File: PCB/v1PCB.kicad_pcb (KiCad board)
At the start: 2 copper layers, 369.9 x 122.3 mm, 218 parts, among them SW1 SW_PUSH, SW2 SW_PUSH, U1 STM32F072CBUx, U2 MCP1700-3302E_SOT23

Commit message: Removed ratsnest, need to fix all runs to vddio, need USB
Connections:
- C1 pad 2: +5V -> GND
- C10 pad 2: +5V -> GND
- C2 pad 2: +5V -> GND
- C3 pad 2: +5V -> GND
- C4 pad 2: +5V -> GND
- C5 pad 2: +5V -> GND
- C6 pad 2: +5V -> GND
- C7 pad 2: +5V -> GND
- C8 pad 2: +5V -> GND
- C9 pad 2: +5V -> GND
- R2 pad 2: +5V -> GND
- SW1 pad 2: +5V -> GND
- U1 pad 23: +5V -> GND
- U1 pad 35: +5V -> GND
- U1 pad 47: +5V -> GND
- U1 pad 49: +5V -> GND
- U1 pad 8: +5V -> GND
- U2 pad 1: +5V -> GND

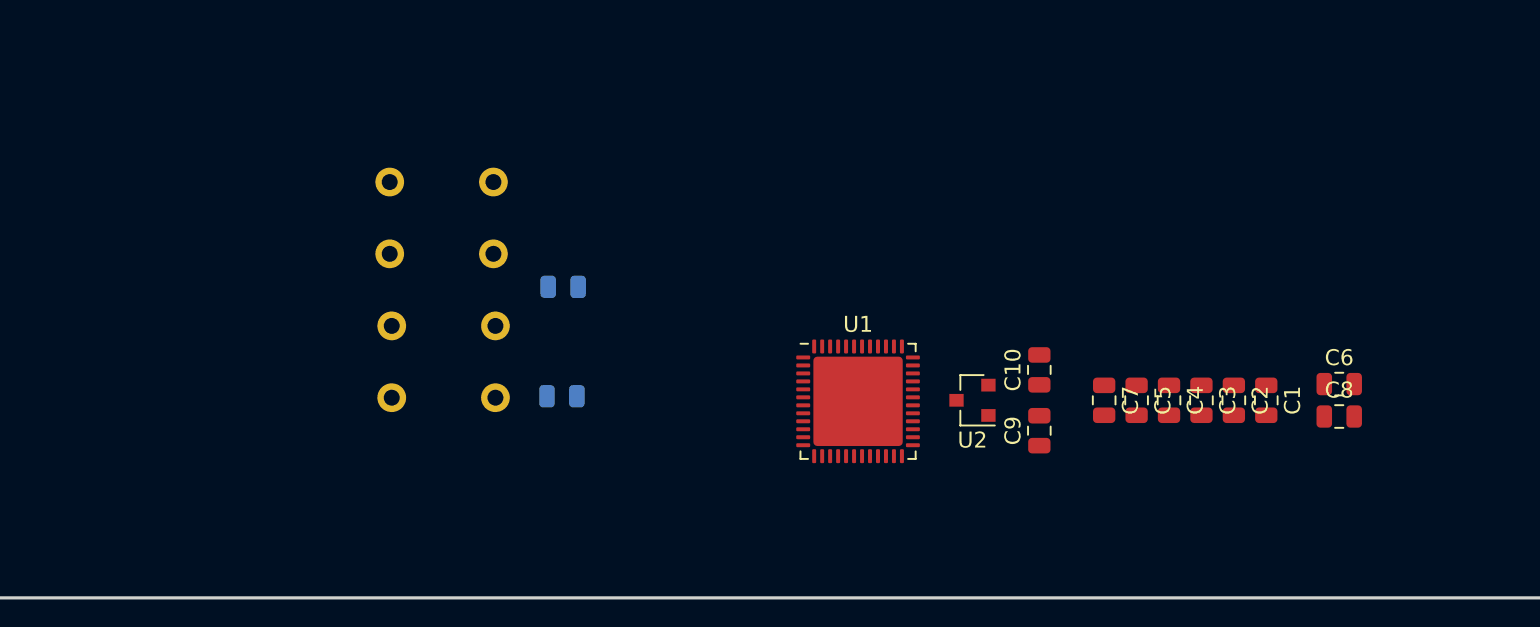
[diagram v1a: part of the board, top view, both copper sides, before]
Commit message: Fixed a few runs, still need to add USB and redo VDDIO decoupling capacitors
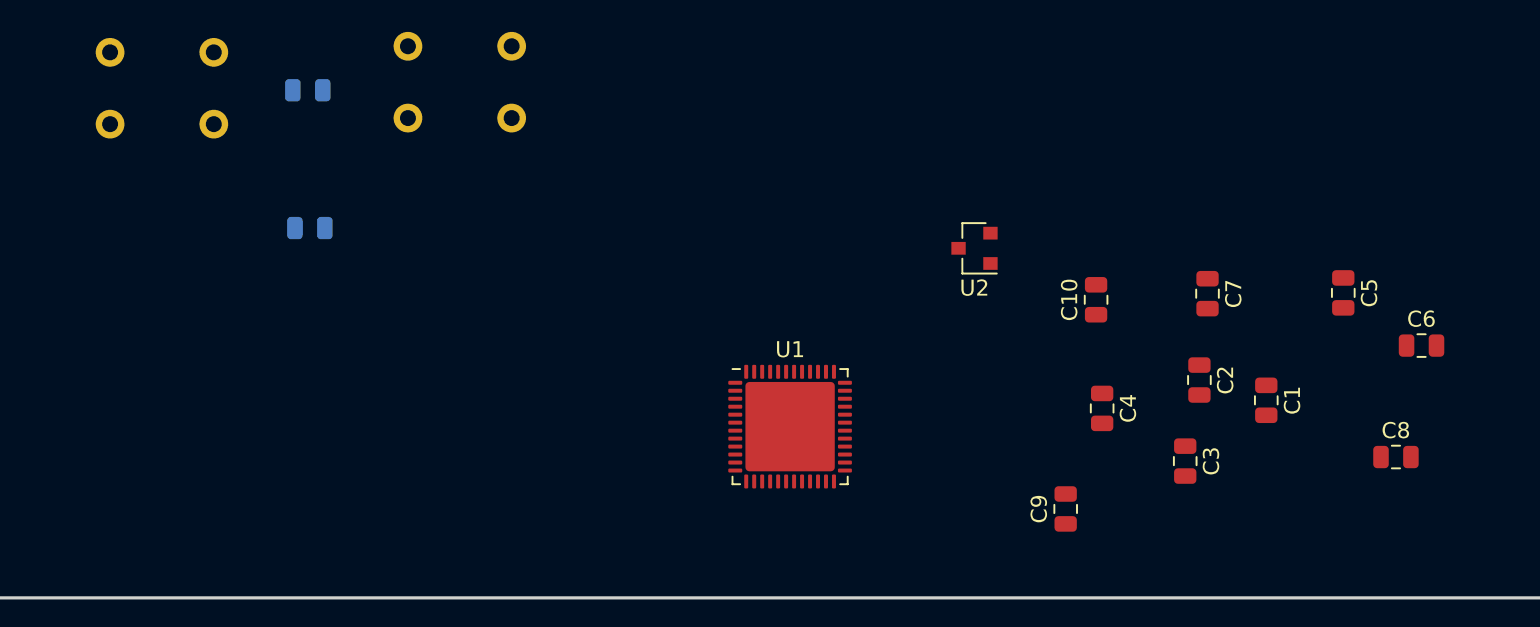
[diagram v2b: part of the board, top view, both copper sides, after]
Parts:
- moved R2 24.9 mm to (222.6, 71.0)
- moved SW2 24.6 mm to (213.5, 70.9)
- moved R1 16.3 mm to (222.8, 79.6)
- moved C5 14.6 mm to (287.5, 83.7)
- moved U2 9.53 mm to (264.4, 80.9)
- moved C7 9.31 mm to (279.0, 83.7)
- moved SW1 8.59 mm to (232.2, 70.5)
- moved C6 5.69 mm to (292.4, 87.0)
- moved C10 5.65 mm to (272.0, 84.1)
- moved C9 5.17 mm to (270.1, 97.2)
- moved U1 4.54 mm to (252.9, 92.1)
- moved C8 4.37 mm to (290.8, 94.0)
- moved C4 4.22 mm to (272.4, 90.9)
- moved C3 3.94 mm to (277.6, 94.2)
- moved C2 2.50 mm to (278.5, 89.2)
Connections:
- U1 pad 10: col16 -> row0
- U1 pad 11: col17 -> row1
- U1 pad 12: col18 -> row2
- U1 pad 13: row0 -> row3
- U1 pad 14: row1 -> row4
- U1 pad 15: row2 -> col8
- U1 pad 16: row3 -> col9
- U1 pad 17: row4 -> col10
- U1 pad 18: col0 -> row5
- U1 pad 19: col1 -> col0
- U1 pad 20: col2 -> col1
- U1 pad 21: col10 -> col2
- U1 pad 22: col11 -> col3
- U1 pad 25: col12 -> col4
- U1 pad 26: col13 -> col5
- U1 pad 27: col14 -> col6
- U1 pad 28: col15 -> col7
- U1 pad 29: row5 -> col11
- U1 pad 30: Net-(U1-Pad30) -> col12
- U1 pad 31: Net-(U1-Pad31) -> col16
- U1 pad 34: Net-(U1-Pad34) -> col17
- U1 pad 37: Net-(U1-Pad37) -> col18
- U1 pad 39: col3 -> Net-(U1-Pad39)
- U1 pad 40: col4 -> Net-(U1-Pad40)
- U1 pad 41: col5 -> Net-(U1-Pad41)
- U1 pad 42: col6 -> Net-(U1-Pad42)
- U1 pad 43: col7 -> Net-(U1-Pad43)
- U1 pad 45: col8 -> Net-(U1-Pad45)
- U1 pad 46: col9 -> Net-(U1-Pad46)

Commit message: Almost done with cap placement, still neeed to add USBC
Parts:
- removed C5: 100uF, Capacitor_SMD:C_0805_2012Metric
- moved R1 99.4 mm to (125.3, 99.4)
- moved R2 99.4 mm to (125.2, 90.8)
- moved SW1 99.4 mm to (134.7, 90.3)
- moved SW2 99.4 mm to (116.1, 90.7)
- moved C6 52.3 mm to (240.5, 93.2), turned to 90 degrees
- moved C8 45.9 mm to (245.0, 93.2), turned to 90 degrees
- moved C9 36.1 mm to (255.5, 64.3), turned to 180 degrees
- moved C1 28.6 mm to (255.4, 98.9), turned to 180 degrees
- moved C4 22.9 mm to (250.2, 85.5), turned to 0 degrees
- moved C7 19.6 mm to (262.8, 94.6)
- moved C3 17.9 mm to (260.4, 89.7)
- moved C10 16.1 mm to (256.9, 78.6), turned to 180 degrees
- moved U2 14.2 mm to (257.0, 68.7), turned to 90 degrees
- moved C2 13.4 mm to (265.1, 89.7)

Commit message: Finished schematic, begin drawing traces
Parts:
- added C5: 4.7nF, Capacitor_SMD:C_0603_1608Metric, F.Cu at (140.5, 108.0)
- added F1: Polyfuse, Fuse:Fuse_1206_3216Metric, B.Cu at (123.0, 106.4)
- added R3: 1M, Resistor_SMD:R_0805_2012Metric, F.Cu at (140.5, 105.6)
- added R4: 5.1k, Resistor_SMD:R_0805_2012Metric, F.Cu at (134.9, 112.7)
- added R5: 5.1k, Resistor_SMD:R_0805_2012Metric, F.Cu at (132.6, 112.7)
- added USB1: HRO-TYPE-C-31-M-12, Type-C:HRO-TYPE-C-31-M-12-Assembly, F.Cu at (133.3, 101.6)
- C1, C3, C4: value 100uF -> 100nF; footprint Capacitor_SMD:C_0805_2012Metric -> Capacitor_SMD:C_0402_1005Metric
- C10: footprint Capacitor_SMD:C_0805_2012Metric -> Capacitor_SMD:C_0402_1005Metric
- C2, C6, C7: footprint Capacitor_SMD:C_0805_2012Metric -> Capacitor_SMD:C_0603_1608Metric
- C8: value 10uF -> 10nF; footprint Capacitor_SMD:C_0805_2012Metric -> Capacitor_SMD:C_0402_1005Metric
- C9: footprint Capacitor_SMD:C_0805_2012Metric -> Capacitor_SMD:C_0402_1005Metric; moved to B.Cu
- K_0, K_1, K_10, K_100, K_11, K_12, K_13, K_14, K_15, K_16, K_17, K_18, K_19, K_2, K_20, K_21, K_22, K_23, K_24, K_25, K_26, K_27, K_28, K_29, K_3, K_30, K_31, K_33, K_34, K_35, K_36, K_38, K_39, K_4, K_40, K_41, K_42, K_43, K_44, K_45, K_46, K_47, K_48, K_49, K_5, K_51, K_52, K_53, K_54, K_56, K_57, K_58, K_59, K_6, K_60, K_61, K_62, K_63, K_64, K_65, K_66, K_68, K_69, K_7, K_70, K_72, K_73, K_74, K_75, K_76, K_77, K_78, K_79, K_8, K_80, K_81, K_83, K_84, K_85, K_86, K_87, K_9, K_96, K_97, K_98, K_99: footprint MX_Alps_Hybrid:MX-1U-NoLED -> MX_Only:MXOnly-1U-NoLED
- K_32: footprint MX_Alps_Hybrid:MX-2U-NoLED -> MX_Only:MXOnly-1U-NoLED
- K_37, K_50: footprint MX_Alps_Hybrid:MX-1.5U-NoLED -> MX_Only:MXOnly-1U-NoLED
- K_55, K_82: footprint MX_Alps_Hybrid:MX-1.75U-NoLED -> MX_Only:MXOnly-1U-NoLED
- K_67, K_71, K_91: footprint MX_Alps_Hybrid:MX-2.25U-NoLED -> MX_Only:MXOnly-1U-NoLED
- K_88, K_89, K_90, K_92, K_94, K_95: footprint MX_Alps_Hybrid:MX-1.25U-NoLED -> MX_Only:MXOnly-1U-NoLED
- K_93: footprint MX_Alps_Hybrid:MX-2.75U-NoLED -> MX_Only:MXOnly-1U-NoLED
- moved C9 156.4 mm to (282.6, 218.3), turned to 90 degrees
- moved U2 152.3 mm to (285.8, 218.3), turned to 0 degrees
- moved C10 143.5 mm to (289.7, 218.3), turned to 90 degrees
- moved C6 141.8 mm to (297.7, 223.0), turned to 180 degrees
- moved C4 139.0 mm to (291.3, 218.3), turned to 90 degrees
- moved C8 138.6 mm to (297.7, 221.5), turned to 180 degrees
- moved U1 131.4 mm to (296.9, 215.9), turned to 90 degrees
- moved C2 129.8 mm to (304.0, 213.5)
- moved C3 125.4 mm to (294.5, 210.3), turned to 0 degrees
- moved C1 123.9 mm to (302.4, 213.5), turned to 270 degrees
- moved C7 118.5 mm to (294.5, 208.8), turned to 0 degrees
- moved SW1 85.9 mm to (218.1, 69.7)
- moved SW2 85.9 mm to (199.4, 70.0)
- moved R1 85.9 mm to (208.7, 78.8)
- moved R2 85.9 mm to (208.6, 70.2)
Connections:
- U1 pad 10: row0 -> Net-(U1-Pad10)
- U1 pad 11: row1 -> Net-(U1-Pad11)
- U1 pad 12: row2 -> Net-(U1-Pad12)
- U1 pad 13: row3 -> Net-(U1-Pad13)
- U1 pad 14: row4 -> Net-(U1-Pad14)
- U1 pad 15: col8 -> Net-(U1-Pad15)
- U1 pad 16: col9 -> Net-(U1-Pad16)
- U1 pad 17: col10 -> Net-(U1-Pad17)
- U1 pad 18: row5 -> Net-(U1-Pad18)
- U1 pad 19: col0 -> Net-(U1-Pad19)
- U1 pad 20: col1 -> Net-(U1-Pad20)
- U1 pad 21: col2 -> Net-(U1-Pad21)
- U1 pad 22: col3 -> Net-(U1-Pad22)
- U1 pad 25: col4 -> Net-(U1-Pad25)
- U1 pad 26: col5 -> Net-(U1-Pad26)
- U1 pad 27: col6 -> Net-(U1-Pad27)
- U1 pad 28: col7 -> Net-(U1-Pad28)
- U1 pad 29: col11 -> Net-(U1-Pad29)
- U1 pad 30: col12 -> Net-(U1-Pad30)
- U1 pad 31: col16 -> Net-(U1-Pad31)
- U1 pad 34: col17 -> Net-(U1-Pad34)
- U1 pad 37: col18 -> Net-(U1-Pad37)
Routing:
- net GND: track 0.00 -> 651.9 mm, vias 0 -> 1
- net +5V: track 0.00 -> 295.6 mm
- net Net-(F1-Pad1): track 0.00 -> 11.4 mm, vias 0 -> 1
- net Net-(C5-Pad2): track 0.00 -> 4.66 mm
- net Net-(R5-Pad2): track 0.00 -> 2.88 mm
- net Net-(R4-Pad2): track 0.00 -> 2.62 mm

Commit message: Need to finish reset buttons, confirm routing of 3V3 and GND, review overall package
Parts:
- F1: value Polyfuse -> Polyfuse (1A)
- R4, R5, USB1: moved to B.Cu
- moved R1 169.4 mm to (300.0, 221.5), turned to 180 degrees
- moved R2 165.3 mm to (288.1, 215.1), turned to 90 degrees
- moved SW1 142.6 mm to (119.1, 172.2)
- moved SW2 122.7 mm to (119.3, 162.9), turned to 180 degrees
- moved D_93 19.4 mm to (269.1, 204.8), turned to 270 degrees
- moved C5 15.0 mm to (126.7, 101.9), turned to 0 degrees
- moved R3 13.8 mm to (126.7, 104.3), turned to 0 degrees
- moved D_67 11.7 mm to (387.4, 173.8)
- moved D_71 11.7 mm to (144.5, 193.0)
- moved D_32 9.32 mm to (389.7, 135.9)
- moved C3 6.95 mm to (294.5, 203.4)
- moved C7 6.95 mm to (294.5, 201.8)
- moved D_55 6.94 mm to (139.7, 173.8)
- moved D_82 6.94 mm to (373.1, 193.0)
- moved C9 6.05 mm to (277.0, 220.7)
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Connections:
- D_54 pad 1: row3 -> row2
- D_87 pad 1: row5 -> row4
- K_32 pad 1: col14 -> col13
- K_38 pad 1: col2 -> col1
- K_39 pad 1: col3 -> col2
- K_40 pad 1: col4 -> col3
- K_41 pad 1: col5 -> col4
- K_42 pad 1: col6 -> col5
- K_43 pad 1: col7 -> col6
- K_44 pad 1: col8 -> col7
- K_45 pad 1: col9 -> col8
- K_46 pad 1: col10 -> col9
- K_47 pad 1: col11 -> col10
- K_48 pad 1: col12 -> col11
- K_49 pad 1: col13 -> col12
- K_56 pad 1: col2 -> col1
- K_57 pad 1: col3 -> col2
- K_58 pad 1: col4 -> col3
- K_59 pad 1: col5 -> col4
- K_60 pad 1: col6 -> col5
- K_61 pad 1: col7 -> col6
- K_62 pad 1: col8 -> col7
- K_63 pad 1: col9 -> col8
- K_64 pad 1: col10 -> col9
- K_65 pad 1: col11 -> col10
- K_66 pad 1: col12 -> col11
- K_71 pad 1: col1 -> col0
- K_72 pad 1: col2 -> col1
- K_73 pad 1: col3 -> col2
- K_74 pad 1: col4 -> col3
- K_75 pad 1: col5 -> col4
- K_76 pad 1: col6 -> col5
- K_77 pad 1: col7 -> col6
- K_78 pad 1: col8 -> col7
- K_79 pad 1: col9 -> col8
- K_80 pad 1: col10 -> col9
- K_81 pad 1: col11 -> col10
- K_82 pad 1: col13 -> col12
- U1 pad 10: Net-(U1-Pad10) -> row0
- U1 pad 11: Net-(U1-Pad11) -> row1
- U1 pad 12: Net-(U1-Pad12) -> row2
- U1 pad 13: Net-(U1-Pad13) -> row3
- U1 pad 14: Net-(U1-Pad14) -> row4
- U1 pad 15: Net-(U1-Pad15) -> row5
- U1 pad 16: Net-(U1-Pad16) -> col18
- U1 pad 17: Net-(U1-Pad17) -> col17
- U1 pad 18: Net-(U1-Pad18) -> col16
- U1 pad 19: Net-(U1-Pad19) -> col15
- U1 pad 20: Net-(U1-Pad20) -> col14
- U1 pad 21: Net-(U1-Pad21) -> col13
- U1 pad 22: Net-(U1-Pad22) -> col12
- U1 pad 25: Net-(U1-Pad25) -> col11
- U1 pad 26: Net-(U1-Pad26) -> col10
- U1 pad 27: Net-(U1-Pad27) -> col9
- U1 pad 28: Net-(U1-Pad28) -> col8
- U1 pad 29: Net-(U1-Pad29) -> col7
- U1 pad 30: Net-(U1-Pad30) -> col6
- U1 pad 37: Net-(U1-Pad37) -> col5
- U1 pad 38: Net-(U1-Pad38) -> col4
- U1 pad 39: Net-(U1-Pad39) -> col3
- U1 pad 40: Net-(U1-Pad40) -> col2
- U1 pad 41: Net-(U1-Pad41) -> col1
- U1 pad 42: Net-(U1-Pad42) -> col0
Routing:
- net row0: track 0.00 -> 624.0 mm, vias 0 -> 1
- net row1: track 0.00 -> 601.9 mm, vias 0 -> 1
- net row2: track 0.00 -> 571.1 mm, vias 0 -> 1
- net row3: track 0.00 -> 551.5 mm, vias 0 -> 1
- net row4: track 0.00 -> 526.5 mm, vias 0 -> 1
- net row5: track 0.00 -> 494.7 mm, vias 0 -> 1
- net GND: track 651.9 -> 348.1 mm, vias 1 -> 4
- net D-: track 0.00 -> 290.3 mm, vias 0 -> 2
- net D+: track 0.00 -> 290.2 mm, vias 0 -> 1
- net col0: track 0.00 -> 280.7 mm
- net col1: track 0.00 -> 265.6 mm
- net col3: track 0.00 -> 260.1 mm
- net col18: track 0.00 -> 257.8 mm
- net col17: track 0.00 -> 243.8 mm
- net col2: track 0.00 -> 243.5 mm
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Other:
- board size 369.9 x 122.3 mm -> 370 x 125.1 mm
- net class Power: trace_width 0.381 -> 0.254

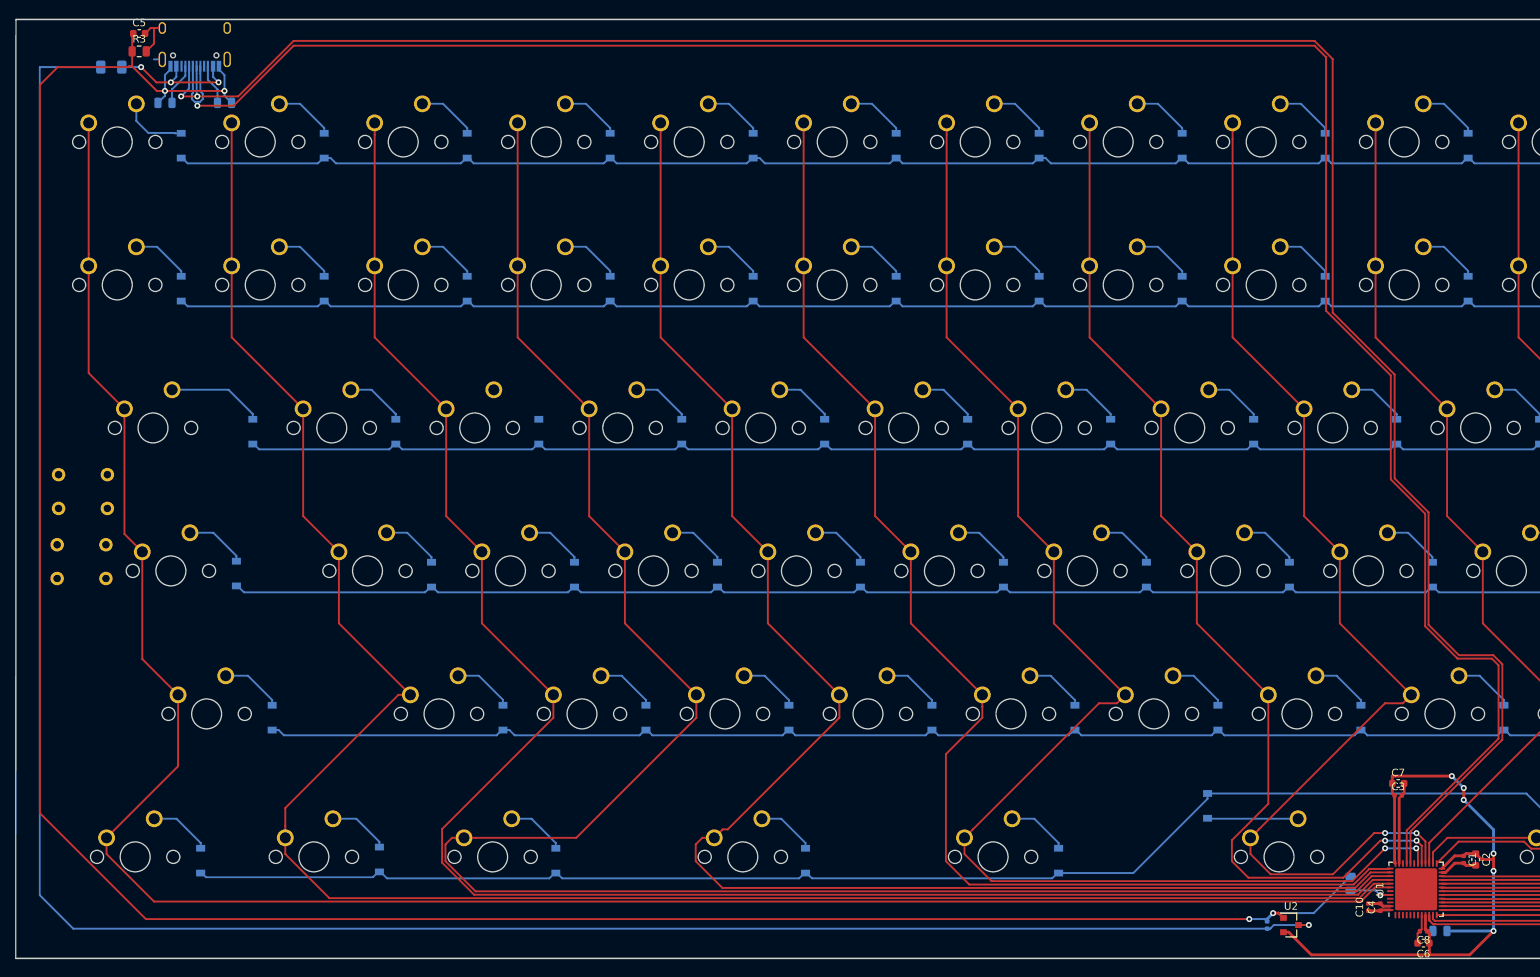
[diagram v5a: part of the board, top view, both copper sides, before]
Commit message: Added switches, fixed most DRC issues. Only questions about GNDleft
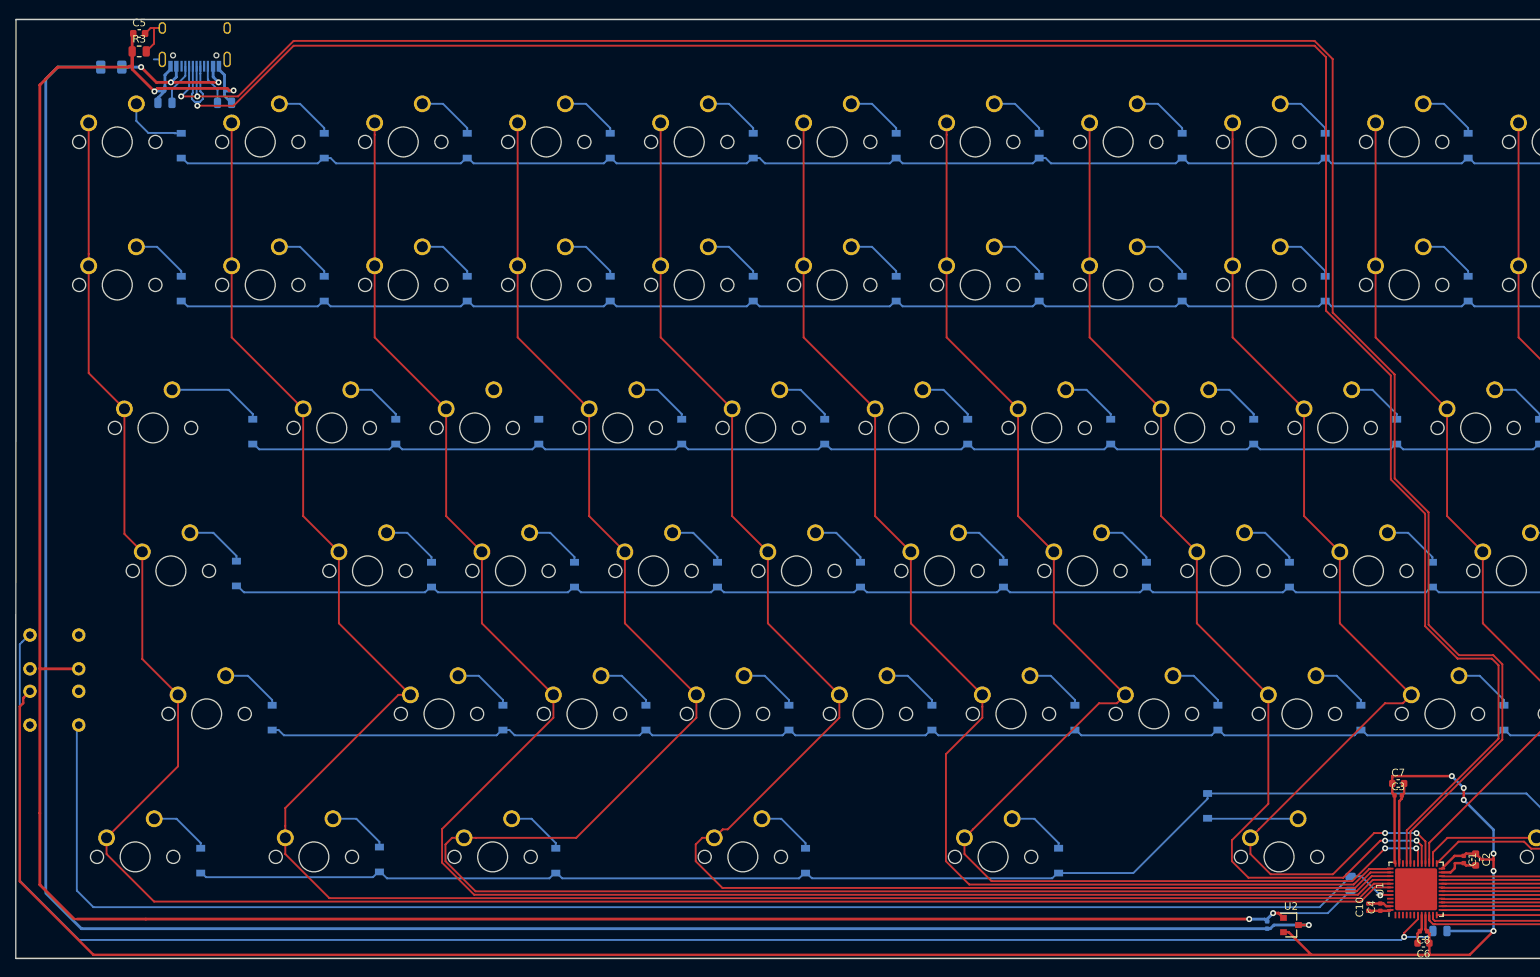
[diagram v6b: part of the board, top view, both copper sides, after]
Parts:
- moved SW2 29.1 mm to (115.4, 191.8), turned to 0 degrees
- moved SW1 12.6 mm to (115.4, 184.3), turned to 180 degrees
- turned R2 to 270 degrees
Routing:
- net NRST: track 0.00 -> 228.9 mm, vias 0 -> 1
- net +3V3: track 96.0 -> 298.0 mm
- net BOOT0: track 5.58 -> 200.7 mm
- net GND: track 348.1 -> 364.7 mm
- net +5V: track 291.0 -> 288.3 mm

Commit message: Review and clean
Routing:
- net GND: track 364.7 -> 451.1 mm, vias 4 -> 10
- net +3V3: track 298.0 -> 317.9 mm, vias 6 -> 8
- net Net-(C5-Pad2): track 7.26 -> 23.2 mm
- net Net-(D_39-Pad2): track 0.00 -> 8.03 mm
- net Net-(F1-Pad1): track 18.6 -> 19.4 mm, vias 3 -> 0
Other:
- net class Power: trace_width 0.254 -> 0.381
